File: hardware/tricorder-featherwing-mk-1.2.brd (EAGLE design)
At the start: 50.8 x 22.9 mm, 10 parts

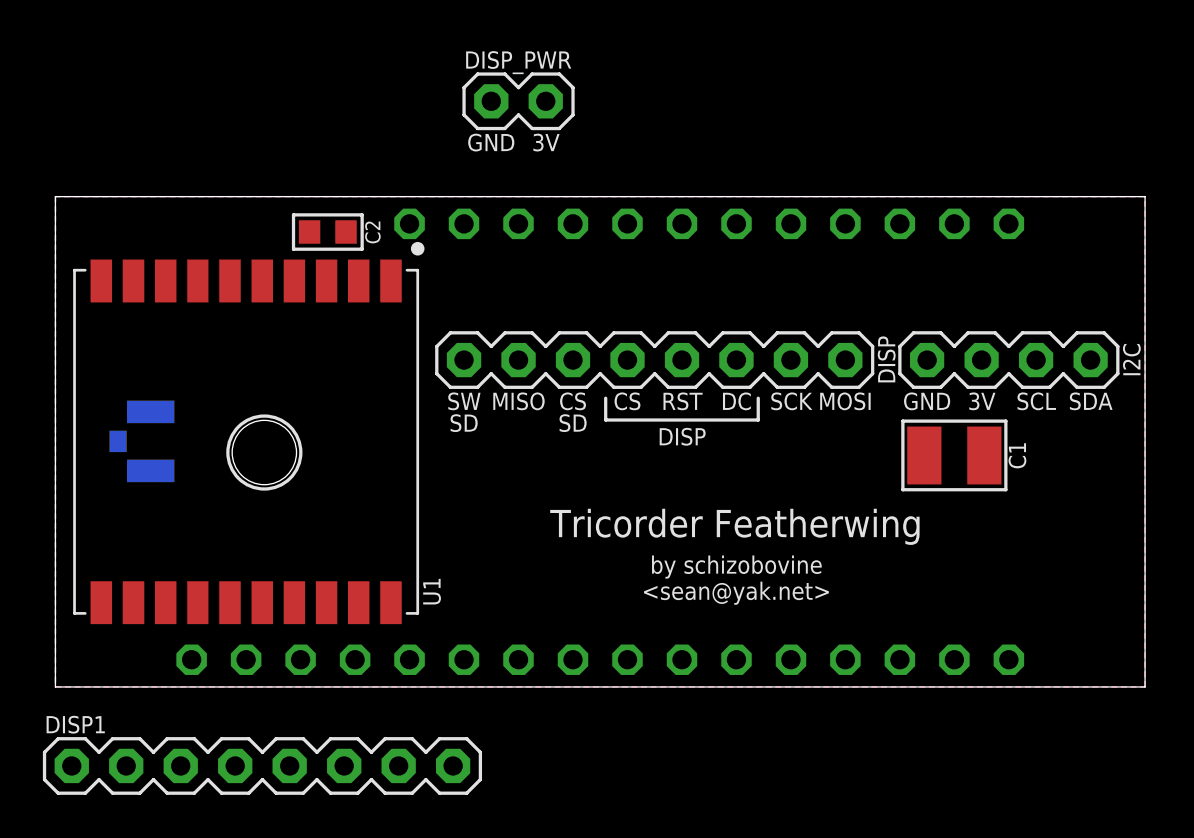
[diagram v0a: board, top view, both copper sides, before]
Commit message: minor tweaks to layout but not done
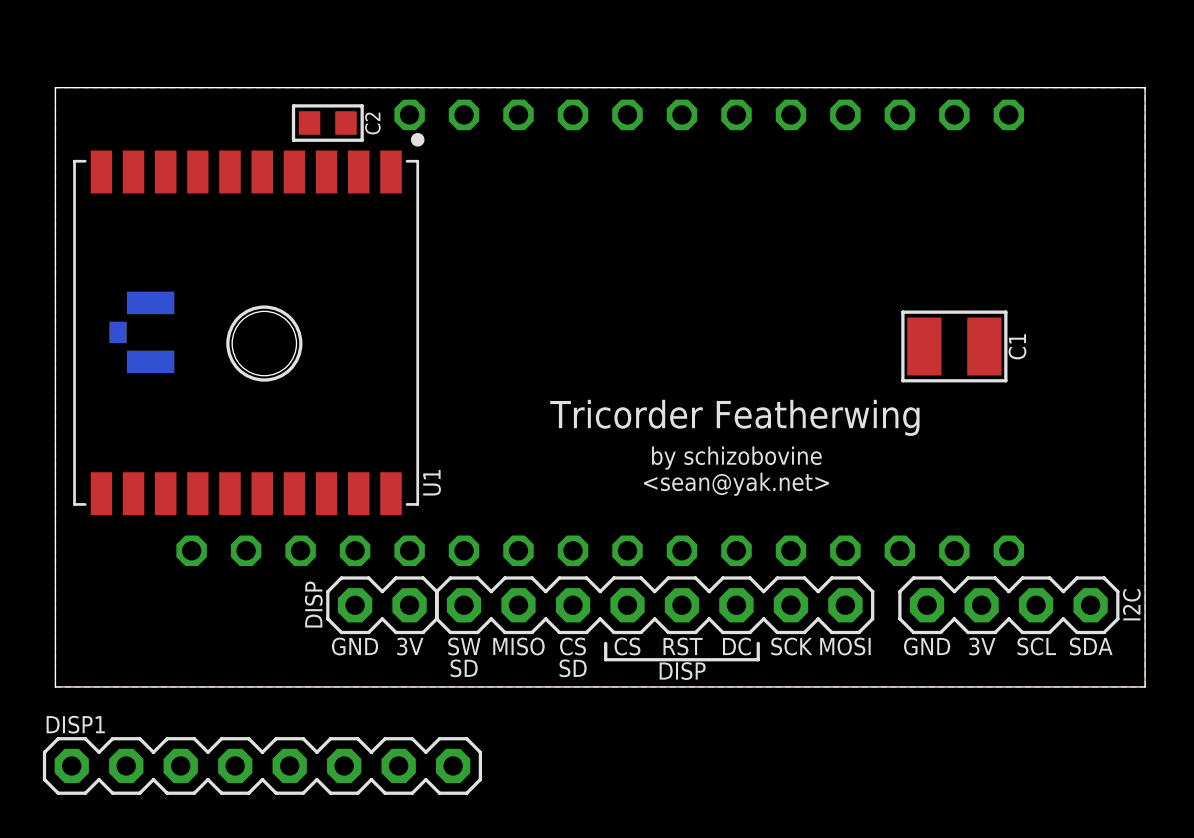
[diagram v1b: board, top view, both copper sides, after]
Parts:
- removed DISP_PWR: M02PTH, a_parts:1X02
- added D_PWR: M02PTH, a_parts:1X02
- moved DISP 11.4 mm to (36.8, 3.81)
- moved I2C 11.4 mm to (40.6, 3.81)
- moved C2 5.08 mm to (12.7, 26.3)
- moved FEATHERWING 5.08 mm to (25.4, 16.5)
- moved U1 5.08 mm to (8.89, 16.5)
- moved C1 5.08 mm to (41.9, 15.9)
- moved GPS_ANT 5.08 mm to (4.45, 16.5)
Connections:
- net 3.3V: now also D_PWR.2; no longer DISP_PWR.2
- net GND: now also D_PWR.1; no longer DISP_PWR.1
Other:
- board size 50.8 x 22.9 mm -> 50.8 x 27.9 mm
